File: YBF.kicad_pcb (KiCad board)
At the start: 2 copper layers, 173.9 x 130.1 mm, 162 parts, among them J1 Chain_LED_out, J2 Chain_LED_return, SW1 1825910-6, SW2 1825910-6

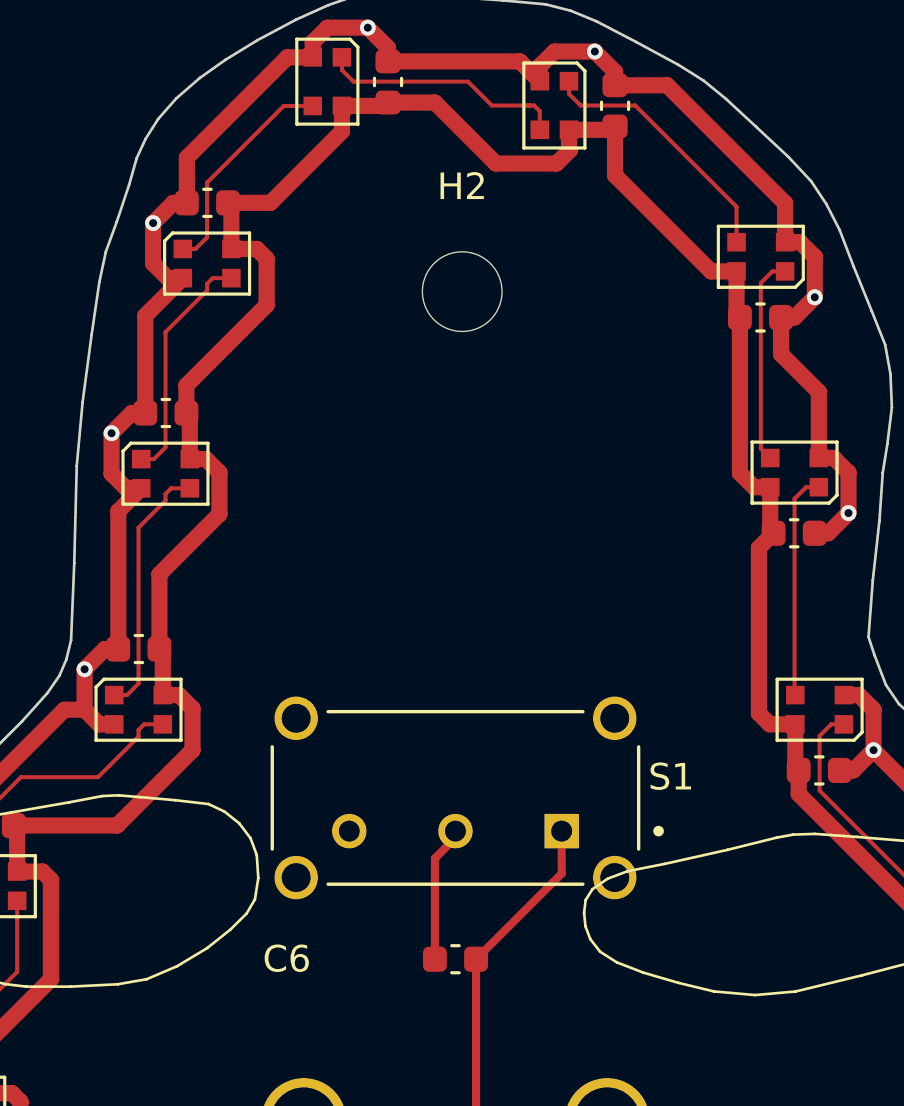
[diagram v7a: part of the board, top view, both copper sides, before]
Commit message: Add chain loop holes
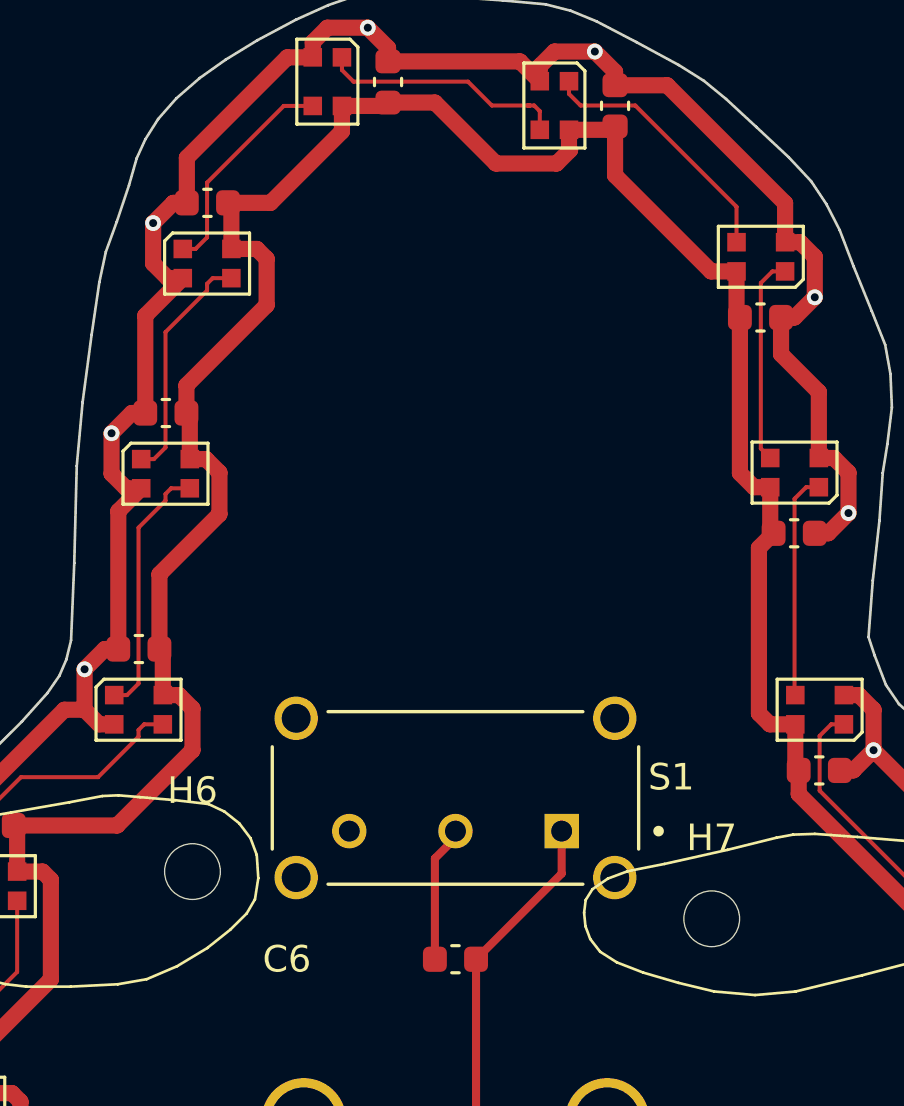
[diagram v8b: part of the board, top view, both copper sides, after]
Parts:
- removed H2: MountingHole, MountingHole:MountingHole_3mm
- added H6: MountingHoleChain1, MountingHole:MountingHole_2.1mm, F.Cu at (135.9, 63.0)
- added H7: MountingHoleChain2, MountingHole:MountingHole_2.1mm, F.Cu at (155.4, 64.8)
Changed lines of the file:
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@@
 		)
 	)
+	(footprint "MountingHole:MountingHole_2.1mm"
+		(layer "F.Cu")
+		(at 155.448 64.77)
+		(descr "Mounting Hole 2.1mm, no annular, generated by kicad-footprint-generator mountinghole.py")
+		(tags "mountinghole")
+		(property "Reference" "H7"
+			(at 0 -3.05 0)
+			(layer "F.SilkS")
+			(effects
+				(font
+					(size 1 1)
+					(thickness 0.15)
+				)
+			)
+		)
+		(property "Value" "MountingHoleChain2"
+			(at 0 3.05 0)
+			(layer "F.Fab")
+			(effects
+				(font
+					(size 1 1)
+					(thickness 0.15)
+				)
+			)
+		)
+		(property "Datasheet" "~"
+			(at 0 0 0)
+			(layer "F.Fab")
+			(hide yes)
+			(effects
+				(font
+					(size 1.27 1.27)
+					(thickness 0.15)
+				)
+			)
+		)
+		(property "Description" "Mounting Hole without connection"
+			(at 0 0 0)
+			(layer "F.Fab")
+			(hide yes)
+			(effects
+				(font
+					(size 1.27 1.27)
+					(thickness 0.15)
+				)
+			)
+		)
+		(property ki_fp_filters "MountingHole*")
+		(sheetname "/")
+		(sheetfile "YBF.kicad_sch")
+		(attr exclude_from_pos_files exclude_from_bom)
+		(fp_circle
+			(center 0 0)
+			(end 2.1 0)
+			(stroke
+				(width 0.15)
+				(type solid)
+			)
+			(fill no)
+			(layer "Cmts.User")
+		)
+		(fp_circle
+			(center 0 0)
+			(end 2.35 0)
+			(stroke
+				(width 0.05)
+				(type solid)
+			)
+			(fill no)
+			(layer "F.CrtYd")
+		)
+		(fp_text user "${REFERENCE}"
+			(at 0 0 0)
+			(layer "F.Fab")
+			(effects
+				(font
+					(size 1 1)
+					(thickness 0.15)
+				)
+			)
+		)
+		(pad "" np_thru_hole circle
+			(at 0 0)
+			(size 2.1 2.1)
+			(drill 2.1)
+			(layers "*.Cu" "*.Mask")
+		)
+		(embedded_fonts no)
+	)
 	(footprint "LED_SMD:LED_WS2812B-2020_PLCC4_2.0x2.0mm"
 		(layer "F.Cu")
@@
 		)
 	)
+	(footprint "MountingHole:MountingHole_2.1mm"
+		(layer "F.Cu")
+		(at 135.89 62.992)
+		(descr "Mounting Hole 2.1mm, no annular, generated by kicad-footprint-generator mountinghole.py")
+		(tags "mountinghole")
+		(property "Reference" "H6"
+			(at 0 -3.05 0)
+			(layer "F.SilkS")
+			(effects
+				(font
+					(size 1 1)
+					(thickness 0.15)
+				)
+			)
+		)
+		(property "Value" "MountingHoleChain1"
+			(at 0 3.05 0)
+			(layer "F.Fab")
+			(effects
+				(font
+					(size 1 1)
+					(thickness 0.15)
+				)
+			)
+		)
+		(property "Datasheet" "~"
+			(at 0 0 0)
+			(layer "F.Fab")
+			(hide yes)
+			(effects
+				(font
+					(size 1.27 1.27)
+					(thickness 0.15)
+				)
+			)
+		)
+		(property "Description" "Mounting Hole without connection"
+			(at 0 0 0)
+			(layer "F.Fab")
+			(hide yes)
+			(effects
+				(font
+					(size 1.27 1.27)
+					(thickness 0.15)
+				)
+			)
+		)
+		(property ki_fp_filters "MountingHole*")
+		(sheetname "/")
+		(sheetfile "YBF.kicad_sch")
+		(attr exclude_from_pos_files exclude_from_bom)
+		(fp_circle
+			(center 0 0)
+			(end 2.1 0)
+			(stroke
+				(width 0.15)
+				(type solid)
+			)
+			(fill no)
+			(layer "Cmts.User")
+		)
+		(fp_circle
+			(center 0 0)
+			(end 2.35 0)
+			(stroke
+				(width 0.05)
+				(type solid)
+			)
+			(fill no)
+			(layer "F.CrtYd")
+		)
+		(fp_text user "${REFERENCE}"
+			(at 0 0 0)
+			(layer "F.Fab")
+			(effects
+				(font
+					(size 1 1)
+					(thickness 0.15)
+				)
+			)
+		)
+		(pad "" np_thru_hole circle
+			(at 0 0)
+			(size 2.1 2.1)
+			(drill 2.1)
+			(layers "*.Cu" "*.Mask")
+		)
+		(embedded_fonts no)
+	)
 	(footprint "LED_SMD:LED_WS2812B-2020_PLCC4_2.0x2.0mm"
 		(layer "F.Cu")
@@
 		)
 	)
-	(footprint "MountingHole:MountingHole_3mm"
-		(layer "F.Cu")
-		(at 146.05 41.148)
-		(descr "Mounting Hole 3mm, no annular, generated by kicad-footprint-generator mountinghole.py")
-		(tags "mountinghole")
-		(property "Reference" "H2"
-			(at 0 -3.95 0)
-			(layer "F.SilkS")
-			(effects
-				(font
-					(size 1 1)
-					(thickness 0.15)
-				)
-			)
-		)
-		(property "Value" "MountingHole"
-			(at 0 3.95 0)
-			(layer "F.Fab")
-			(effects
-				(font
-					(size 1 1)
-					(thickness 0.15)
-				)
-			)
-		)
-		(property "Datasheet" "~"
-			(at 0 0 0)
-			(layer "F.Fab")
-			(hide yes)
-			(effects
-				(font
-					(size 1.27 1.27)
-					(thickness 0.15)
-				)
-			)
-		)
-		(property "Description" "Mounting Hole without connection"
-			(at 0 0 0)
-			(layer "F.Fab")
-			(hide yes)
-			(effects
-				(font
-					(size 1.27 1.27)
-					(thickness 0.15)
-				)
-			)
-		)
-		(property ki_fp_filters "MountingHole*")
-		(sheetname "/")
-		(sheetfile "YBF.kicad_sch")
-		(attr exclude_from_pos_files exclude_from_bom)
-		(fp_circle
-			(center 0 0)
-			(end 3 0)
-			(stroke
-				(width 0.15)
-				(type solid)
-			)
-			(fill no)
-			(layer "Cmts.User")
-		)
-		(fp_circle
-			(center 0 0)
-			(end 3.25 0)
-			(stroke
-				(width 0.05)
-				(type solid)
-			)
-			(fill no)
-			(layer "F.CrtYd")
-		)
-		(fp_text user "${REFERENCE}"
-			(at 0 0 0)
-			(layer "F.Fab")
-			(effects
-				(font
-					(size 1 1)
-					(thickness 0.15)
-				)
-			)
-		)
-		(pad "" np_thru_hole circle
-			(at 0 0)
-			(size 3 3)
-			(drill 3)
-			(layers "*.Cu" "*.Mask")
-		)
-		(embedded_fonts no)
-	)
 	(footprint "Capacitor_SMD:C_0603_1608Metric"
